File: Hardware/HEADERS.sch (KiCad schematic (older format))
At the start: 23 parts, among them J16 SPOX-3, J17 SPOX-3, J18 SPOX-4, J20 SPOX-3, J22 SPOX-3, J23 SPOX-5, J24 SPOX-5, J25 SPOX-4, J26 SPOX-4, J27 SPOX-4, J28 SPOX-6, J29 SPOX-6, J31 SPOX-6, J33 SPOX-6, J34 SPOX-6, J35 SPOX-6, J36 SPOX-6

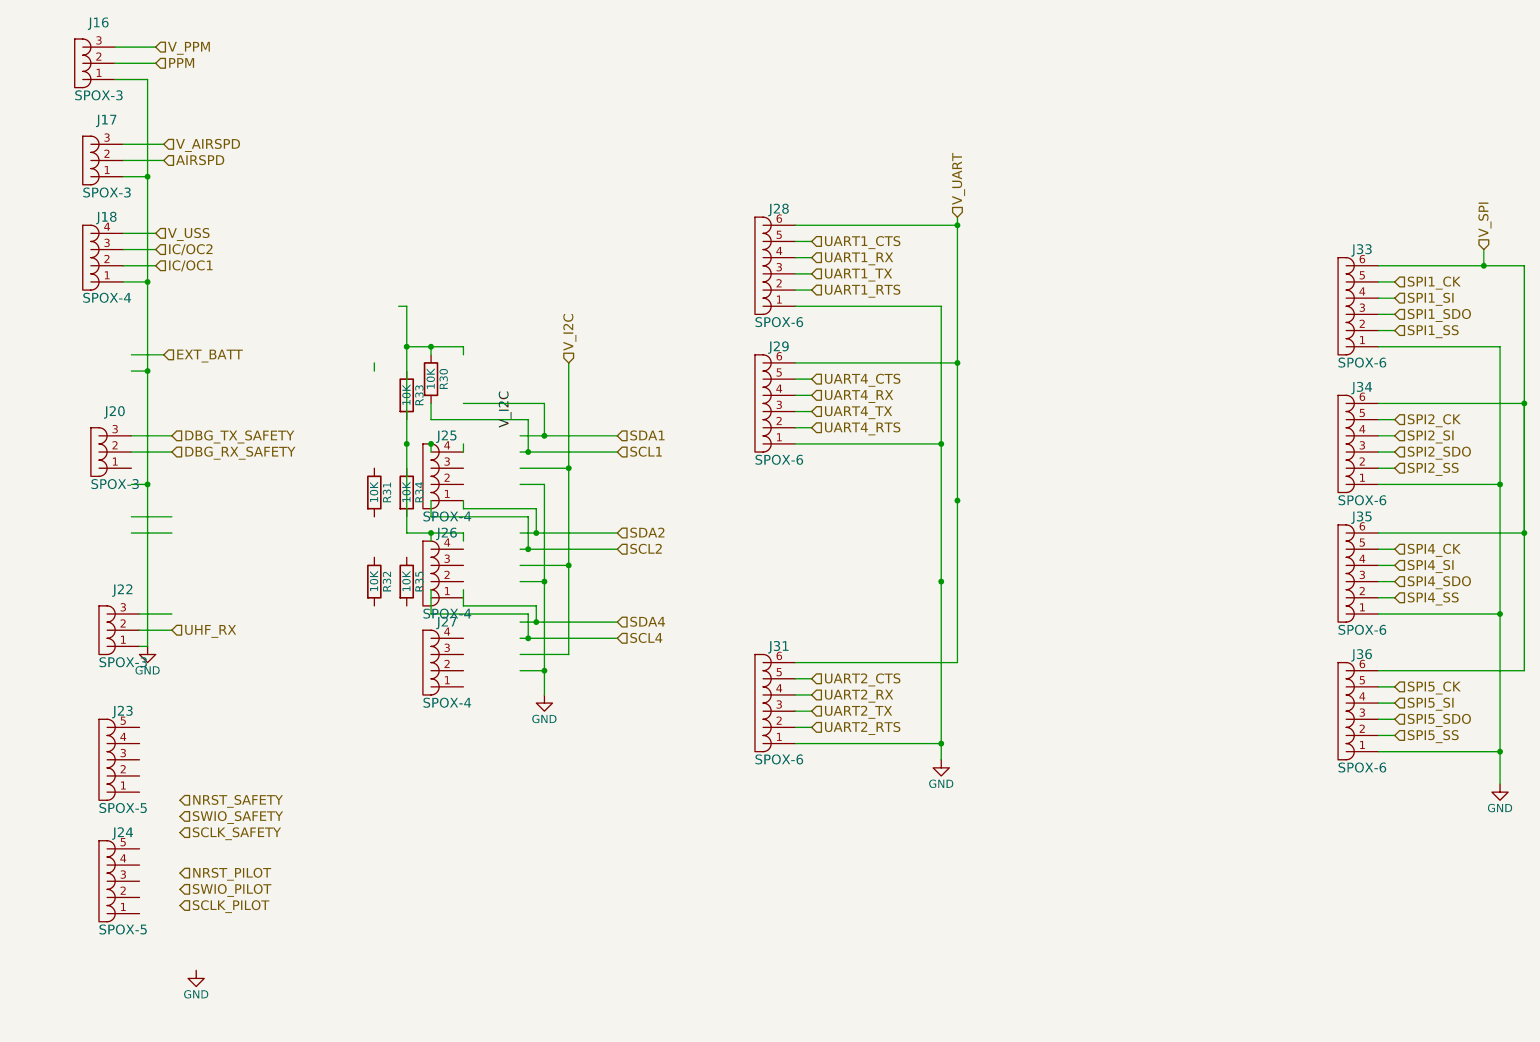
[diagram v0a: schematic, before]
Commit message: Fixed HEADERS.sch file
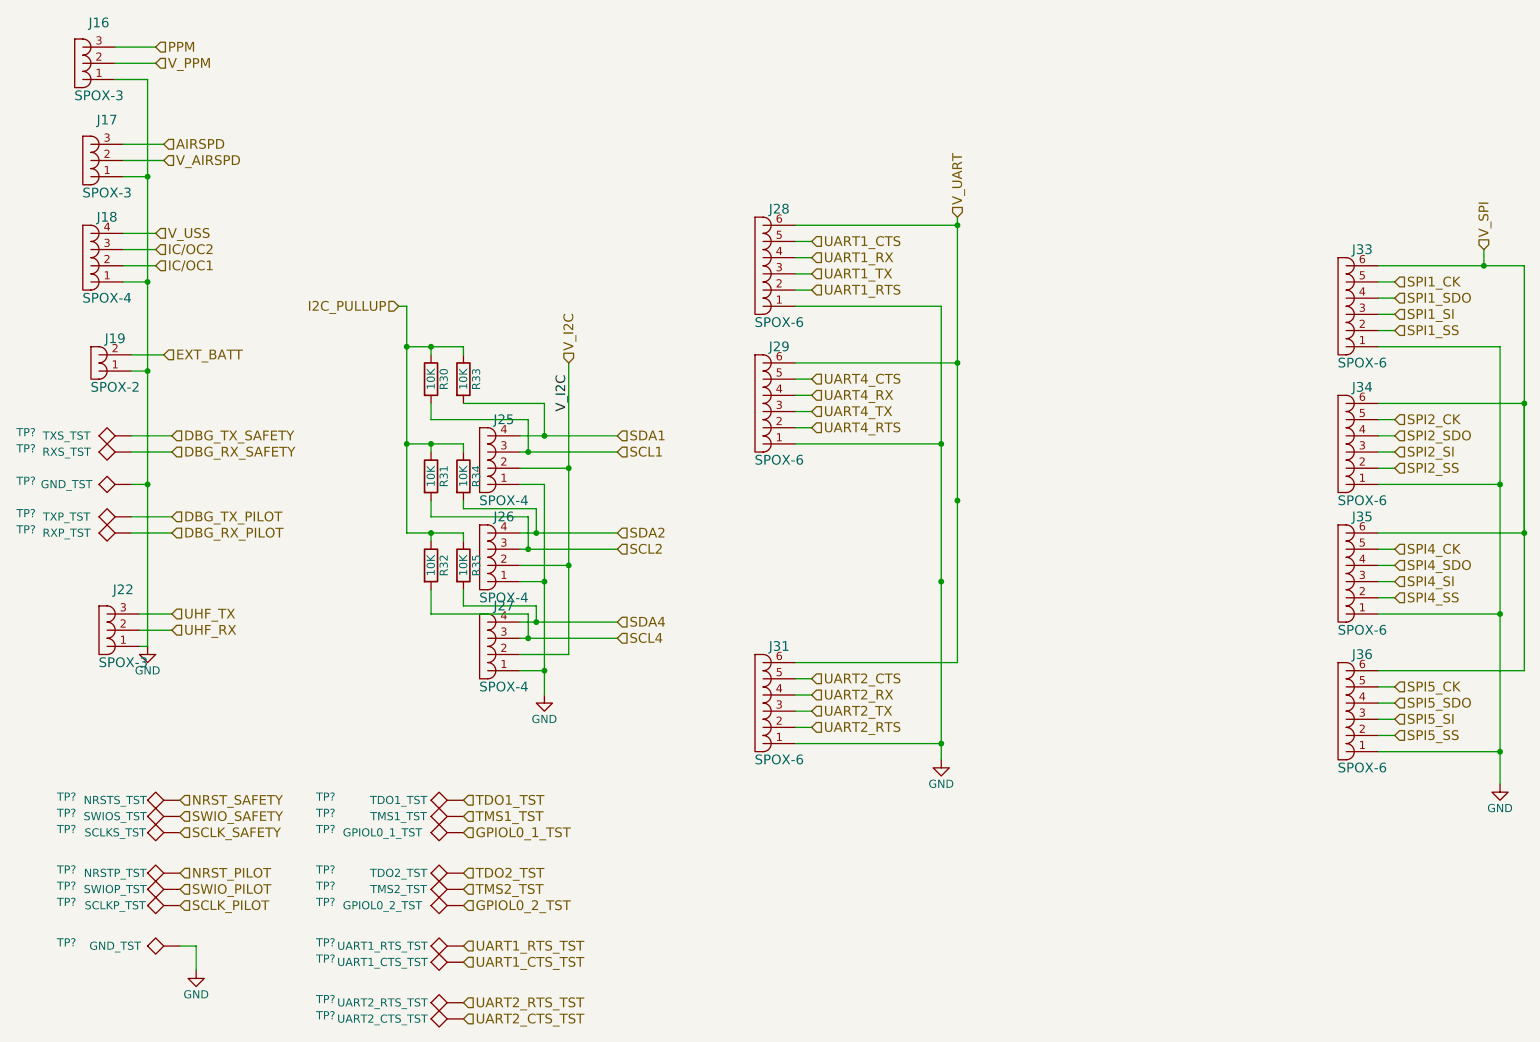
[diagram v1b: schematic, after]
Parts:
- removed J20: SPOX-3, Connectors_Molex:Molex_SPOX-5267_22-03-5035_03x2.54mm_Straight, symbol SPOX-3
- removed J23, J24: SPOX-5, Connectors_Molex:Molex_SPOX-5267_22-03-5055_05x2.54mm_Straight, symbol SPOX-5
- added J19: SPOX-2, Connectors_Molex:Molex_SPOX-5267_22-03-5025_02x2.54mm_Straight, symbol SPOX-2
- added TP?: TDO1_TST, Measurement_Points:Measurement_Point_Round-SMD-Pad_Small, symbol TEST
- added TP?: TMS1_TST, Measurement_Points:Measurement_Point_Round-SMD-Pad_Small, symbol TEST
- added TP?: GPIOL0_1_TST, Measurement_Points:Measurement_Point_Round-SMD-Pad_Small, symbol TEST
- added TP?: TDO2_TST, Measurement_Points:Measurement_Point_Round-SMD-Pad_Small, symbol TEST
- added TP?: TMS2_TST, Measurement_Points:Measurement_Point_Round-SMD-Pad_Small, symbol TEST
- added TP?: GPIOL0_2_TST, Measurement_Points:Measurement_Point_Round-SMD-Pad_Small, symbol TEST
- added TP?: UART1_RTS_TST, Measurement_Points:Measurement_Point_Round-SMD-Pad_Small, symbol TEST
- added TP?: UART1_CTS_TST, Measurement_Points:Measurement_Point_Round-SMD-Pad_Small, symbol TEST
- added TP?: UART2_RTS_TST, Measurement_Points:Measurement_Point_Round-SMD-Pad_Small, symbol TEST
- added TP?: UART2_CTS_TST, Measurement_Points:Measurement_Point_Round-SMD-Pad_Small, symbol TEST
- added TP?: TXS_TST, Measurement_Points:Measurement_Point_Round-SMD-Pad_Small, symbol TEST
- added TP?: RXS_TST, Measurement_Points:Measurement_Point_Round-SMD-Pad_Small, symbol TEST
- added TP?: TXP_TST, Measurement_Points:Measurement_Point_Round-SMD-Pad_Small, symbol TEST
- added TP?: RXP_TST, Measurement_Points:Measurement_Point_Round-SMD-Pad_Small, symbol TEST
- added TP? (x2): GND_TST, Measurement_Points:Measurement_Point_Round-SMD-Pad_Small, symbol TEST
- added TP?: NRSTS_TST, Measurement_Points:Measurement_Point_Round-SMD-Pad_Small, symbol TEST
- added TP?: SWIOS_TST, Measurement_Points:Measurement_Point_Round-SMD-Pad_Small, symbol TEST
- added TP?: SCLKS_TST, Measurement_Points:Measurement_Point_Round-SMD-Pad_Small, symbol TEST
- added TP?: SWIOP_TST, Measurement_Points:Measurement_Point_Round-SMD-Pad_Small, symbol TEST
- added TP?: SCLKP_TST, Measurement_Points:Measurement_Point_Round-SMD-Pad_Small, symbol TEST
- added TP?: NRSTP_TST, Measurement_Points:Measurement_Point_Round-SMD-Pad_Small, symbol TEST
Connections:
- net labels added: DBG_RX_PILOT, DBG_TX_PILOT, GPIOL0_1_TST, GPIOL0_2_TST, I2C_PULLUP, TDO1_TST, TDO2_TST, TMS1_TST, TMS2_TST, UART1_CTS_TST, UART1_RTS_TST, UART2_CTS_TST, UART2_RTS_TST, UHF_TX
- wire segments 111 -> 113
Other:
- moved on the sheet: J25, J26, J27, R31, R32, R33, R34, R35

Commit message: Fixed merge issues
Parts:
- gave numbers to parts that had none: 22
- renumbered J22 to J20, J25 to J21, J26 to J22, J27 to J23, J28 to J24, J29 to J25, J31 to J26, J33 to J27, J34 to J28, J35 to J29, J36 to J30, R30 to R47, R31 to R48, R32 to R49, R33 to R50, R34 to R51, R35 to R52

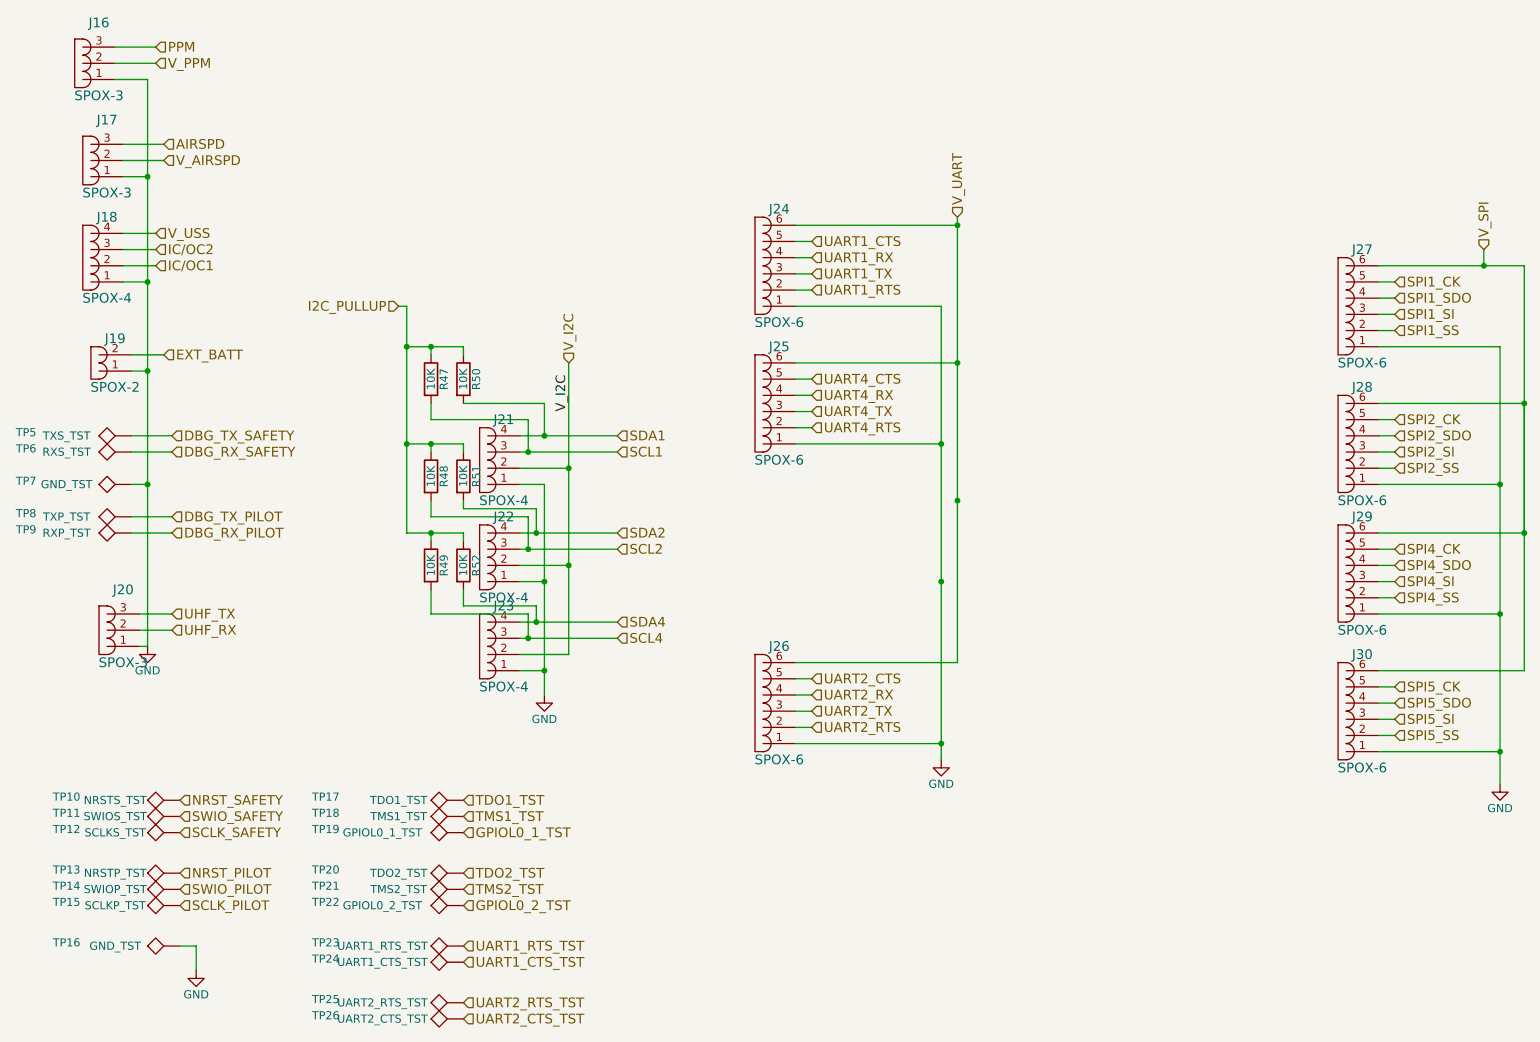
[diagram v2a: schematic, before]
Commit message: Removed unused connectors, started placements of components on new board
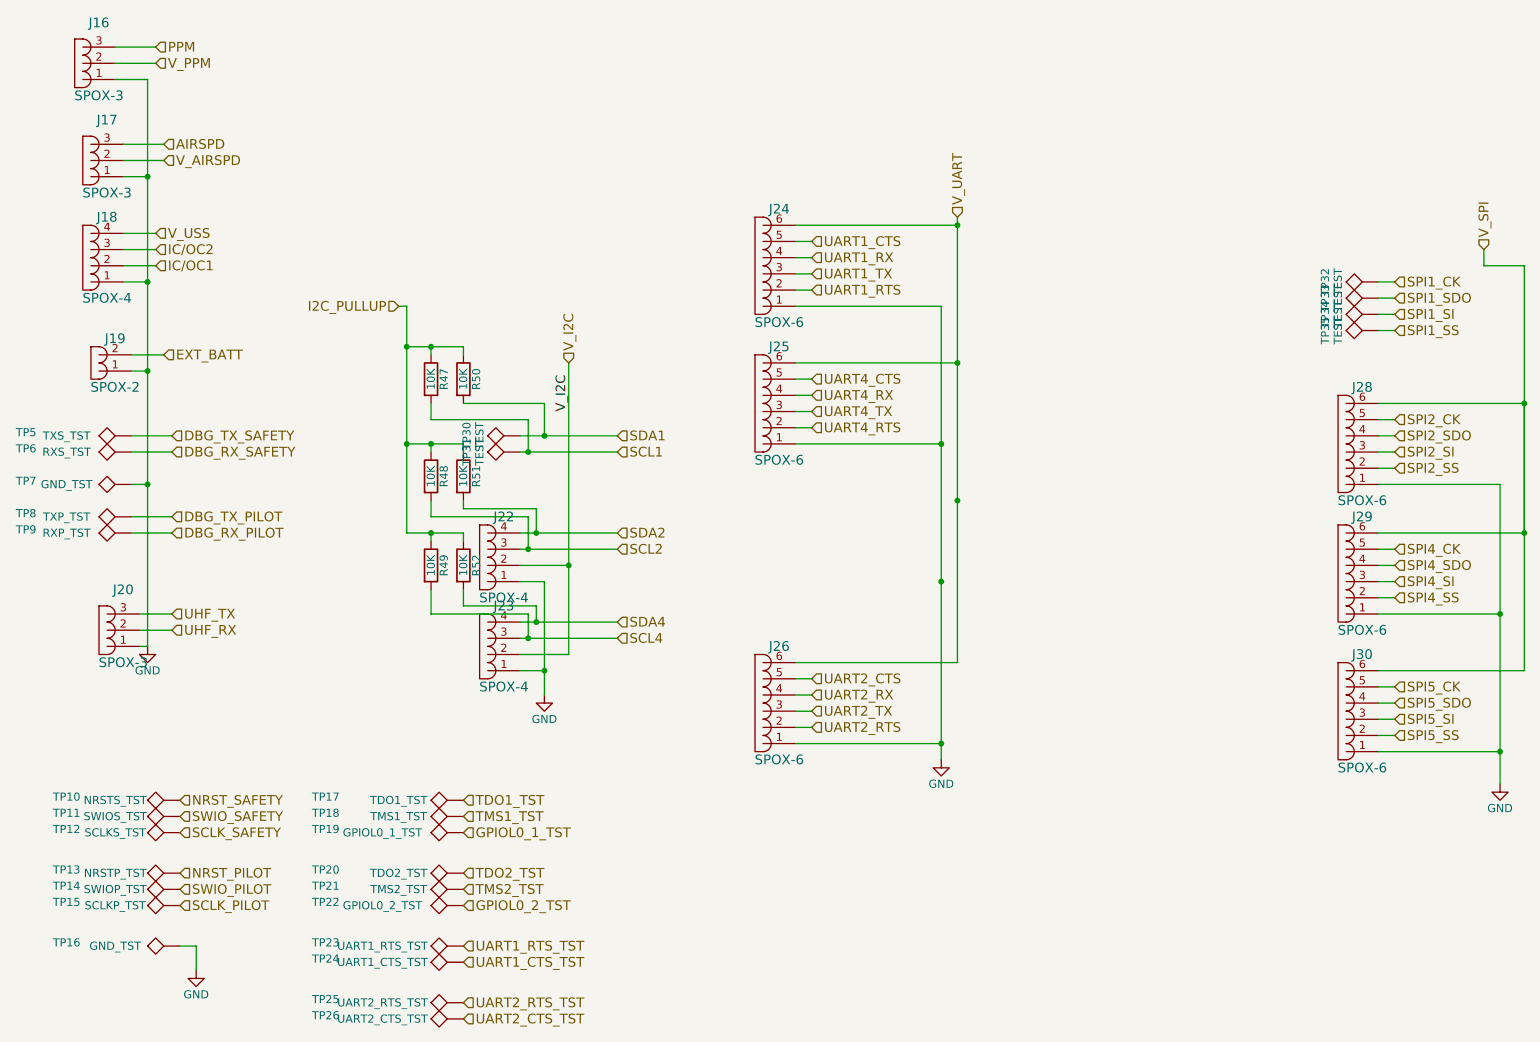
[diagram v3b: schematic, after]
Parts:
- removed J21: SPOX-4, Connectors_Molex:Molex_SPOX-5267_22-03-5045_04x2.54mm_Straight, symbol SPOX-4
- removed J27: SPOX-6, Connectors_Molex:Molex_SPOX-5267_22-03-5065_06x2.54mm_Straight, symbol SPOX-6
- added TP30, TP31, TP32, TP33, TP34, TP35: TEST, Measurement_Points:Measurement_Point_Round-SMD-Pad_Small, symbol TEST
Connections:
- net SCL1: now also TP31.1
- net SDA1: now also TP30.1
- net SPI1_CK: now also TP32.1
- net SPI1_SDO: now also TP33.1
- net SPI1_SI: now also TP34.1
- net SPI1_SS: now also TP35.1
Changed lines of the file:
@@
-$EndComp
-$Comp
-L SPOX-6 J27
-U 1 1 595BDD44
-P 9000 2900
-F 0 "J27" H 9100 3250 60  0000 C CNN
-F 1 "SPOX-6" H 9100 2550 60  0000 C CNN
-F 2 "Connectors_Molex:Molex_SPOX-5267_22-03-5065_06x2.54mm_Straight" H 9000 3050 60  0001 C CNN
-F 3 "" H 9000 3050 60  0001 C CNN
-F 4 "CONN-005" H 9200 3350 60  0001 C CNN "part_num"
-	1    9000 2900
-	1    0    0    -1
 $EndComp
 $Comp
@@
 $EndComp
 $Comp
-L SPOX-4 J21
-U 1 1 595C301B
-P 3700 3850
-F 0 "J21" H 3800 4100 60  0000 C CNN
-F 1 "SPOX-4" H 3800 3600 60  0000 C CNN
-F 2 "Connectors_Molex:Molex_SPOX-5267_22-03-5045_04x2.54mm_Straight" H 3700 3900 60  0001 C CNN
-F 3 "" H 3700 3900 60  0001 C CNN
-F 4 "CONN-003" H 3900 4200 60  0001 C CNN "part_num"
-	1    3700 3850
-	1    0    0    -1
-$EndComp
-$Comp
 L SPOX-4 J22
 U 1 1 595C306F
@@
 	1750 3800 1500 3800
 Wire Wire Line
-	3900 4000 4050 4000
-Wire Wire Line
-	4050 4000 4050 5300
+	4050 4600 4050 5300
 Wire Wire Line
 	4050 5150 3900 5150
 Wire Wire Line
 	3900 4600 4050 4600
-Connection ~ 4050 4600
 Connection ~ 4050 5150
 Wire Wire Line
@@
 	3900 4500 4200 4500
 Connection ~ 4200 4500
-Connection ~ 4200 3900
 Wire Wire Line
 	3900 3700 4500 3700
@@
 Wire Wire Line
 	3900 4950 4500 4950
-Wire Wire Line
-	3900 3900 4200 3900
 Wire Wire Line
 	5600 2900 6500 2900
@@
 	9300 3050 9200 3050
 Wire Wire Line
-	9200 2650 10100 2650
+	9850 2650 10100 2650
 Wire Wire Line
 	10100 3500 10100 4300
 Wire Wire Line
-	9200 3150 9950 3150
-Wire Wire Line
-	9950 3150 9950 5850
+	9950 4000 9950 5850
 Wire Wire Line
 	9850 2550 9850 2650
-Connection ~ 9850 2650
 Connection ~ 10100 3500
 Connection ~ 10100 4300
@@
 Wire Wire Line
 	9200 4000 9950 4000
-Connection ~ 9950 4000
 Wire Wire Line
 	3350 3500 3350 3600
@@
 Text HLabel 3550 7300 2    60   Input ~ 0
 UART2_CTS_TST
+$Comp
+L TEST TP32
+U 1 1 5B3C0C72
+P 9200 2750
+F 0 "TP32" H 9200 3050 50  0000 C BNN
+F 1 "TEST" H 9200 3000 50  0000 C CNN
+F 2 "Measurement_Points:Measurement_Point_Round-SMD-Pad_Small" H 9200 2750 50  0001 C CNN
+F 3 "" H 9200 2750 50  0001 C CNN
+	1    9200 2750
+	0    -1   -1   0
+$EndComp
+$Comp
+L TEST TP33
+U 1 1 5B3C0F1B
+P 9200 2850
+F 0 "TP33" H 9200 3150 50  0000 C BNN
+F 1 "TEST" H 9200 3100 50  0000 C CNN
+F 2 "Measurement_Points:Measurement_Point_Round-SMD-Pad_Small" H 9200 2850 50  0001 C CNN
+F 3 "" H 9200 2850 50  0001 C CNN
+	1    9200 2850
+	0    -1   -1   0
+$EndComp
+$Comp
+L TEST TP34
+U 1 1 5B3C1148
+P 9200 2950
+F 0 "TP34" H 9200 3250 50  0000 C BNN
+F 1 "TEST" H 9200 3200 50  0000 C CNN
+F 2 "Measurement_Points:Measurement_Point_Round-SMD-Pad_Small" H 9200 2950 50  0001 C CNN
+F 3 "" H 9200 2950 50  0001 C CNN
+	1    9200 2950
+	0    -1   -1   0
+$EndComp
+$Comp
+L TEST TP35
+U 1 1 5B3C1282
+P 9200 3050
+F 0 "TP35" H 9200 3350 50  0000 C BNN
+F 1 "TEST" H 9200 3300 50  0000 C CNN
+F 2 "Measurement_Points:Measurement_Point_Round-SMD-Pad_Small" H 9200 3050 50  0001 C CNN
+F 3 "" H 9200 3050 50  0001 C CNN
+	1    9200 3050
+	0    -1   -1   0
+$EndComp
+$Comp
+L TEST TP30
+U 1 1 5B3C1DA0
+P 3900 3700
+F 0 "TP30" H 3900 4000 50  0000 C BNN
+F 1 "TEST" H 3900 3950 50  0000 C CNN
+F 2 "Measurement_Points:Measurement_Point_Round-SMD-Pad_Small" H 3900 3700 50  0001 C CNN
+F 3 "" H 3900 3700 50  0001 C CNN
+	1    3900 3700
+	0    -1   -1   0
+$EndComp
+$Comp
+L TEST TP31
+U 1 1 5B3C21DB
+P 3900 3800
+F 0 "TP31" H 3900 4100 50  0000 C BNN
+F 1 "TEST" H 3900 4050 50  0000 C CNN
+F 2 "Measurement_Points:Measurement_Point_Round-SMD-Pad_Small" H 3900 3800 50  0001 C CNN
+F 3 "" H 3900 3800 50  0001 C CNN
+	1    3900 3800
+	0    -1   -1   0
+$EndComp
 $EndSCHEMATC
